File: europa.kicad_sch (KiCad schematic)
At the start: 16 parts, among them J1 Left, J2 Right, J3 AudioJack2_Ground, J4 AudioJack2_Ground, J5 AudioJack2_Ground, J6 AudioJack2_Ground

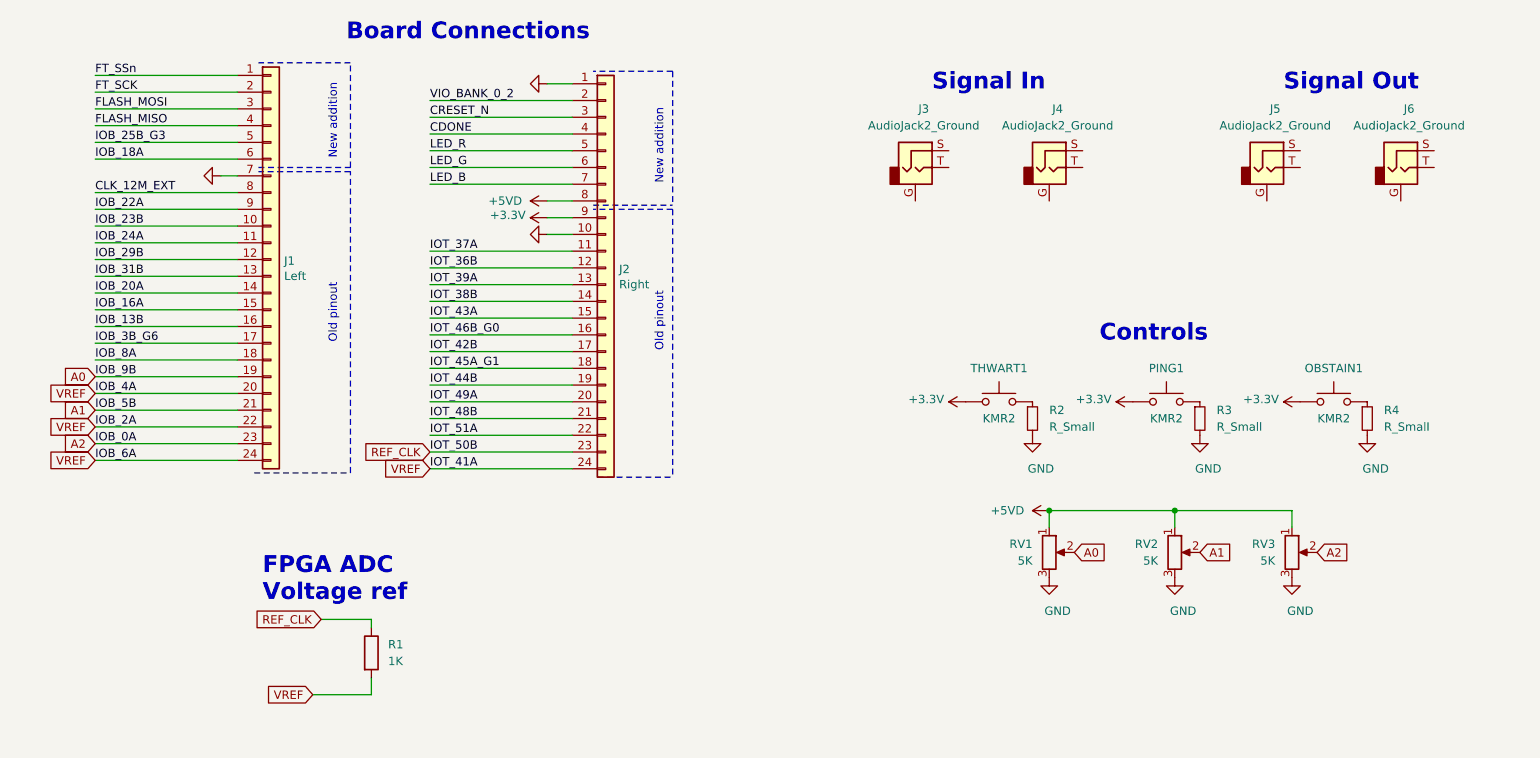
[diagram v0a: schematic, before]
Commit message: Layout finished, needs tweak in proper components
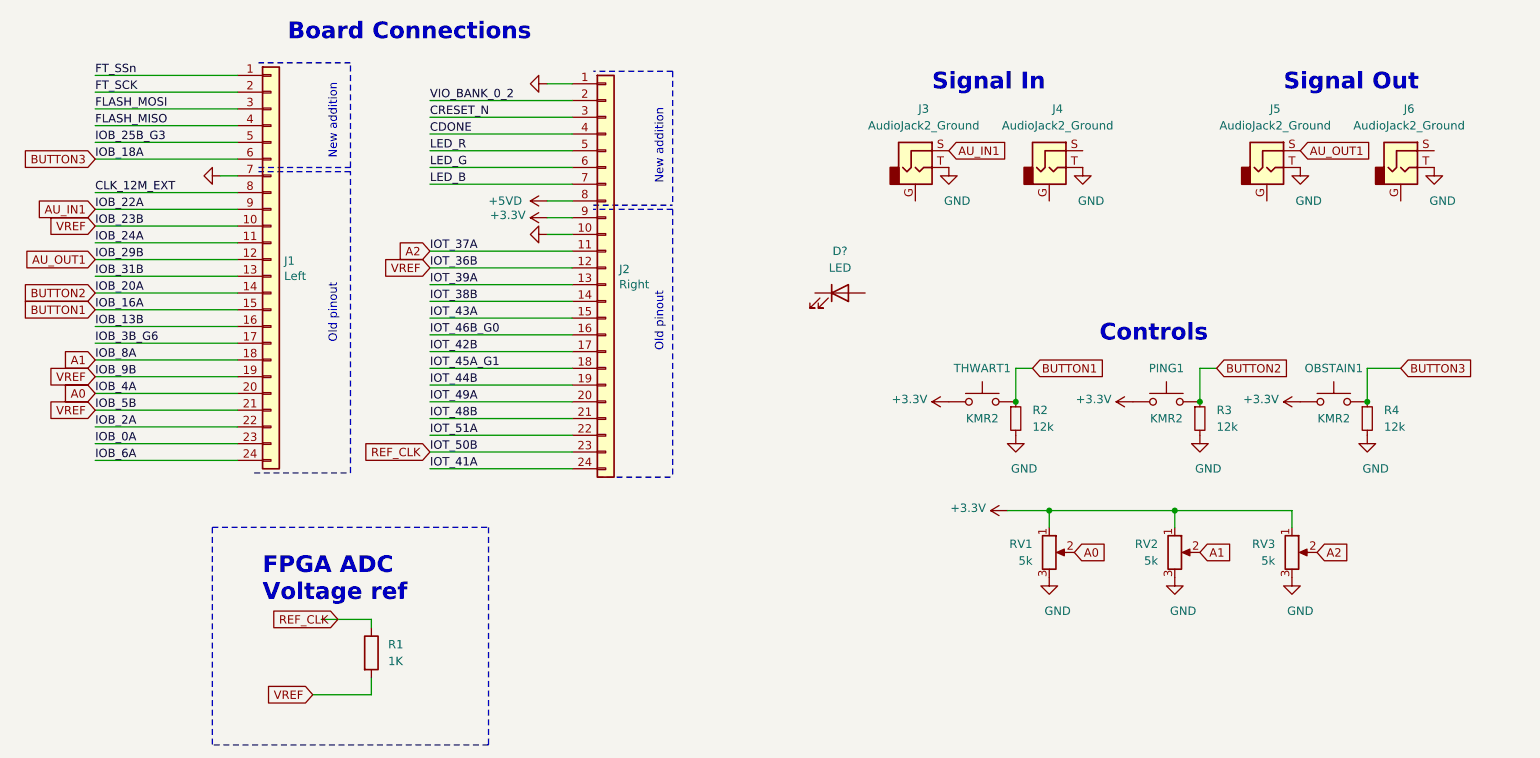
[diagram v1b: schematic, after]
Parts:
- added D?: LED, LED_THT:LED_D5.0mm, symbol Device:LED
- R2, R3, R4: value R_Small -> 12k
- RV1, RV2, RV3: value 5K -> 5k
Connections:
- net IOB_16A is gone; now on net BUTTON1: J1.15 (Pin_15)
- net IOB_18A is gone; now on net BUTTON3: J1.6 (Pin_6)
- net IOB_20A is gone; now on net BUTTON2: J1.14 (Pin_14)
- net IOB_22A is gone; now on net AU_IN1: J1.9 (Pin_9)
- net IOB_23B is gone; now on net VREF: J1.10 (Pin_10)
- net IOB_29B is gone; now on net AU_OUT1: J1.12 (Pin_12)
- net IOB_8A is gone; now on net A1: J1.18 (Pin_18)
- net IOT_36B is gone; now on net VREF: J2.12 (Pin_12)
- net IOT_37A is gone; now on net A2: J2.11 (Pin_11)
- net +3V3: now also RV1.1, RV2.1, RV3.1
- net +5VD: no longer RV1.1, RV2.1, RV3.1
- net A0: now also J1.20 (Pin_20); no longer J1.19 (Pin_19)
- net A1: no longer J1.21 (Pin_21)
- net A2: no longer J1.23 (Pin_23)
- net GND: now also J3.T, J4.T, J5.T, J6.T
- net VREF: now also J1.19 (Pin_19), J1.21 (Pin_21); no longer J1.20 (Pin_20), J1.22 (Pin_22), J1.24 (Pin_24), J2.24 (Pin_24)
- net BUTTON1: now reaches R2.1, THWART1.1
- net AU_OUT1: now reaches J5.S
- net BUTTON2: now reaches PING1.1, R3.1
- net AU_IN1: now reaches J3.S
- net BUTTON3: now reaches OBSTAIN1.1, R4.1
- new net IOB_0A: J1.23 (Pin_23)
- new net IOB_2A: J1.22 (Pin_22)
- new net IOB_6A: J1.24 (Pin_24)
- new net IOT_41A: J2.24 (Pin_24)
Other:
- moved on the sheet: R2, THWART1

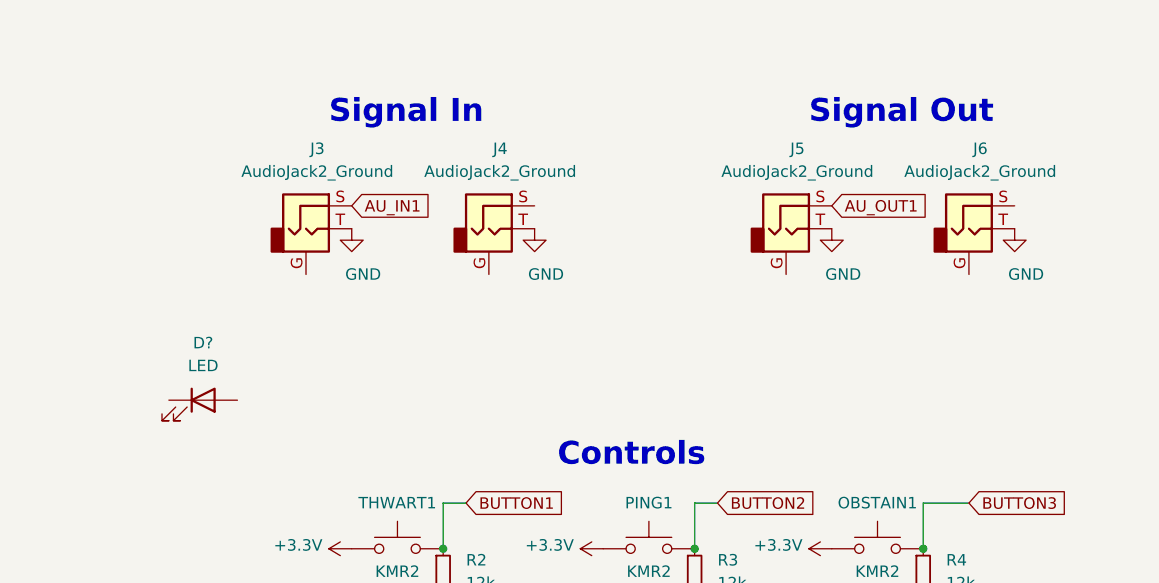
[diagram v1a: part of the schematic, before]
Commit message: Mono plugs now connecting properly. Switches found at farnell
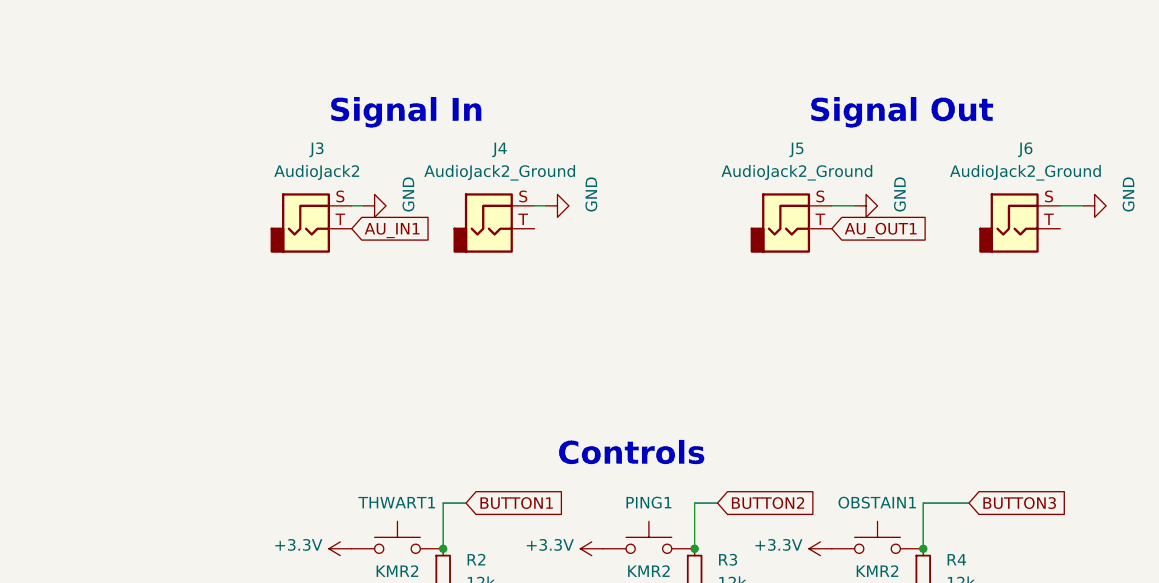
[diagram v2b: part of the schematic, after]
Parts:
- removed D?: LED, LED_THT:LED_D5.0mm, symbol Device:LED
- J3: value AudioJack2_Ground -> AudioJack2; symbol Connector:AudioJack2_Ground -> Connector:AudioJack2
- J4, J5, J6: symbol Connector:AudioJack2_Ground -> Connector:AudioJack2
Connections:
- net AU_IN1: now also J3.T; no longer J3.S
- net AU_OUT1: now also J5.T; no longer J5.S
- net GND: now also J3.S, J4.S, J5.S, J6.S; no longer J3.T, J4.T, J5.T, J6.T
